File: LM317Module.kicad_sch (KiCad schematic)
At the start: 9 parts, among them J1 Input, J3 Digital VA measure, J7 Output, Q1 BD139, Q3 TIP2955G, U1 LM317

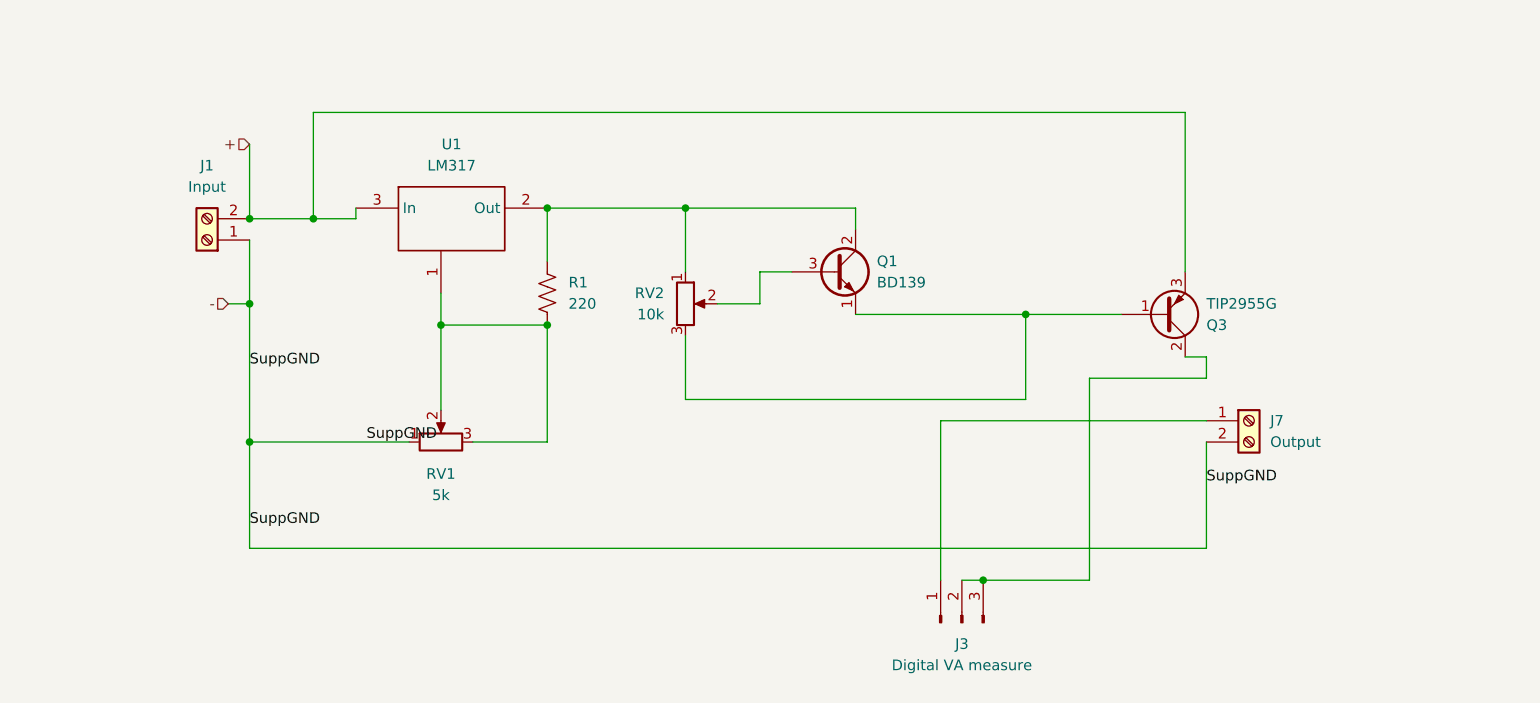
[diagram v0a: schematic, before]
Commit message: Updates to the schematic to make use of the centre tapped transformer to get negative rail.
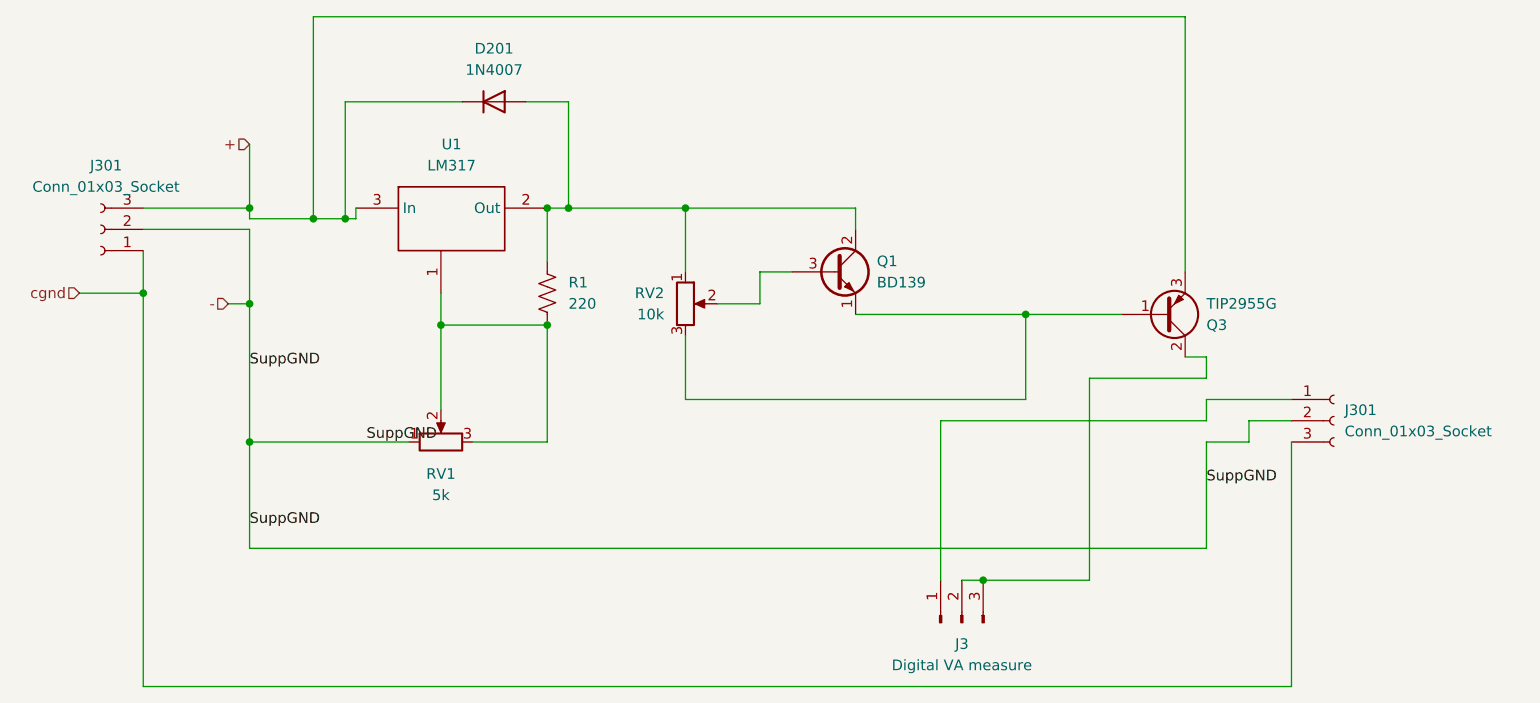
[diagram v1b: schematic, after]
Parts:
- removed J1: Input, TerminalBlock_Phoenix:TerminalBlock_Phoenix_MKDS-1,5-2-5.08_1x02_P5.08mm_Horizontal, symbol Connector:Screw_Terminal_01x02
- removed J7: Output, TerminalBlock_Phoenix:TerminalBlock_Phoenix_MKDS-1,5-2-5.08_1x02_P5.08mm_Horizontal, symbol Connector:Screw_Terminal_01x02
- added D201: 1N4007, Diode_THT:D_DO-41_SOD81_P10.16mm_Horizontal, symbol Diode:1N4007
- added J301 (x2): Conn_01x03_Socket, symbol Connector:Conn_01x03_Socket
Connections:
- net +: now also D201.1 (K), J301.3 (Pin_3)
- net -: now also J301.2 (Pin_2), J301.2 (Pin_2)
- net at Q1.2 (C), R1.1, RV2.1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: now also D201.2 (A)
- net at J3.1 (Pin_1): now also J301.1 (Pin_1)
- new net cgnd: J301.1 (Pin_1), J301.3 (Pin_3)
